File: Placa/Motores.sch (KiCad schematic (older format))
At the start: 11 parts, among them U1 DVR8833, U2 DVR8833

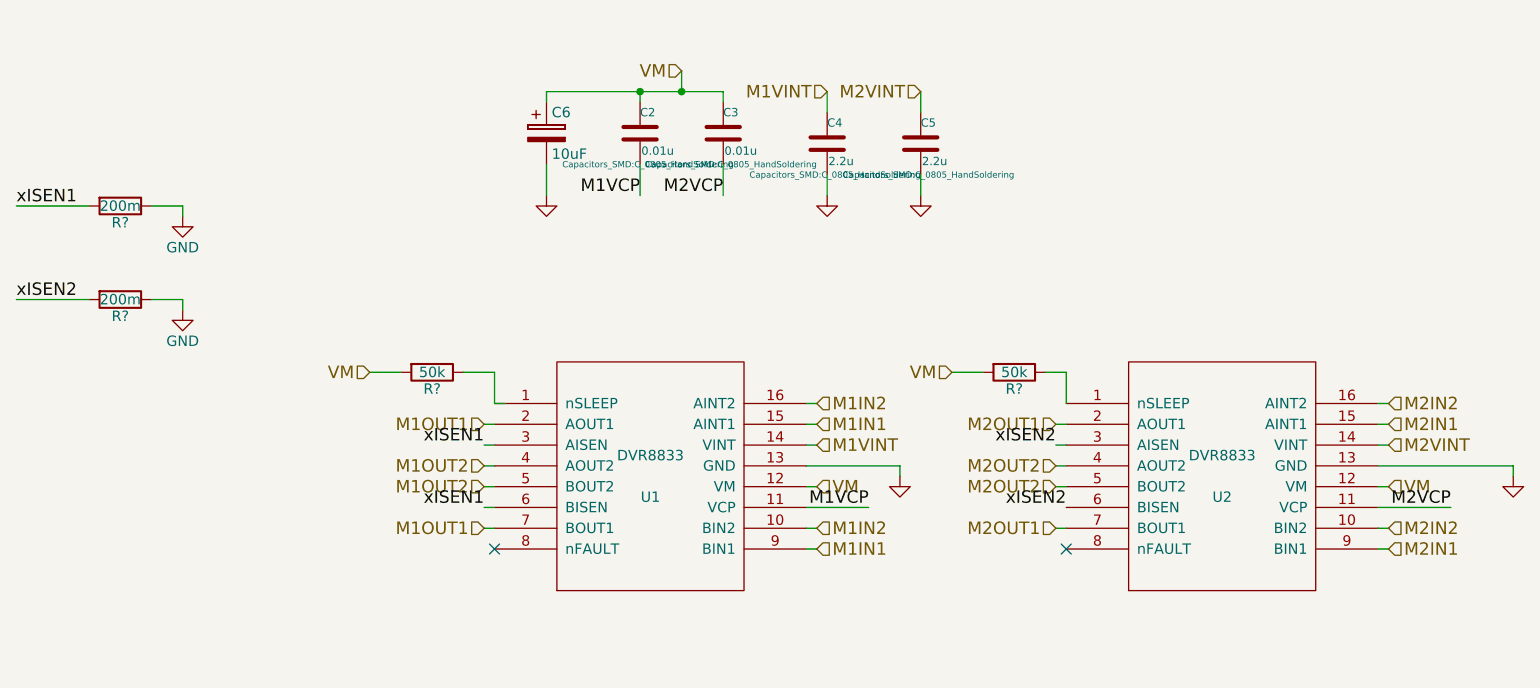
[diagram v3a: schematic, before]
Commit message: estan casi todas las cosas en su lugar, falta cambiar DVRs y regulador y rutear
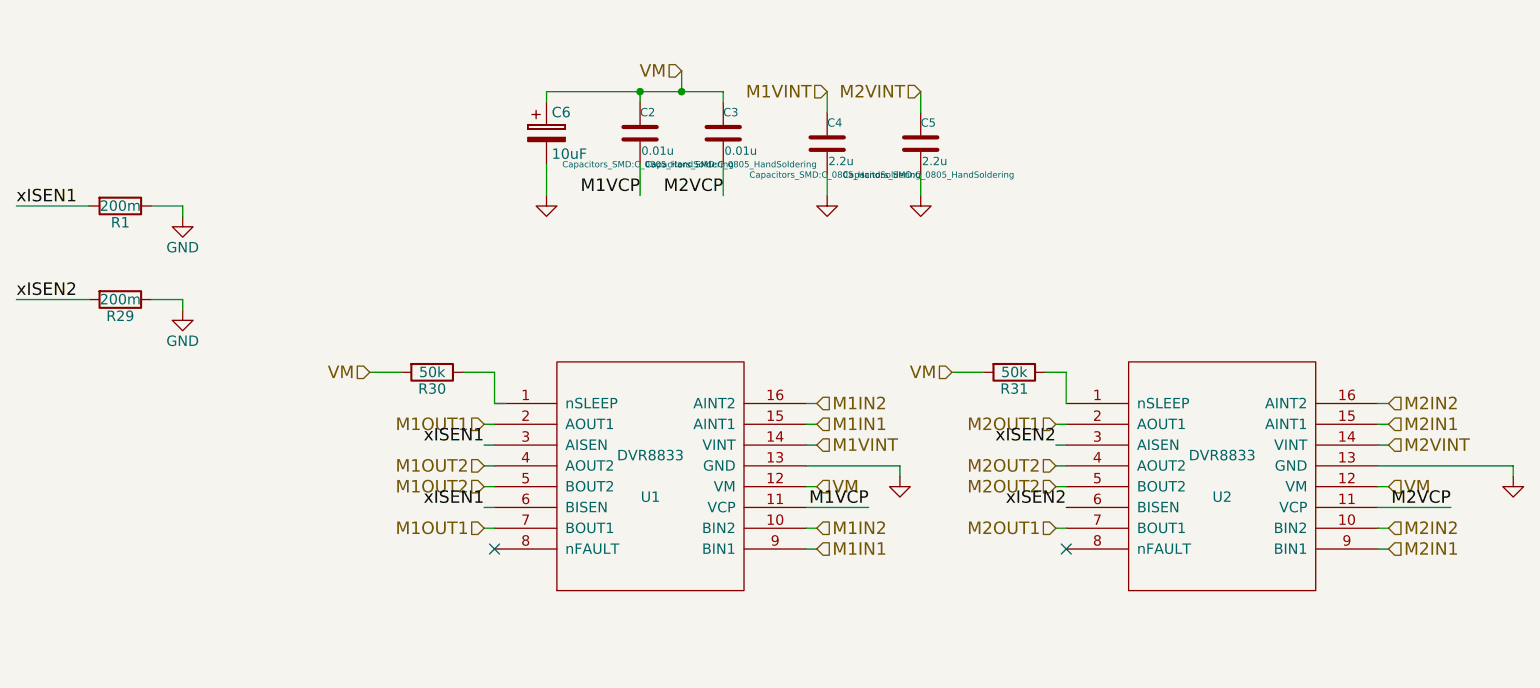
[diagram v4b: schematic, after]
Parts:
- gave numbers to parts that had none: 4
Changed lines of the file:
@@
 $EndComp
 $Comp
-L GND #PWR043
+L GND #PWR43
 U 1 1 55EB047B
 P 5600 3800
-F 0 "#PWR043" H 5600 3800 30  0001 C CNN
+F 0 "#PWR43" H 5600 3800 30  0001 C CNN
 F 1 "GND" H 5600 3730 30  0001 C CNN
 F 2 "" H 5600 3800 60  0000 C CNN
@@
 $EndComp
 $Comp
-L GND #PWR044
+L GND #PWR45
 U 1 1 55EB0487
 P 8550 3800
-F 0 "#PWR044" H 8550 3800 30  0001 C CNN
+F 0 "#PWR45" H 8550 3800 30  0001 C CNN
 F 1 "GND" H 8550 3730 30  0001 C CNN
 F 2 "" H 8550 3800 60  0000 C CNN
@@
 	4350 2300 4350 2450
 $Comp
-L GND #PWR045
+L GND #PWR41
 U 1 1 55EB1201
 P 3900 2450
-F 0 "#PWR045" H 3900 2450 30  0001 C CNN
+F 0 "#PWR41" H 3900 2450 30  0001 C CNN
 F 1 "GND" H 3900 2380 30  0001 C CNN
 F 2 "" H 3900 2450 60  0000 C CNN
@@
 $EndComp
 $Comp
-L GND #PWR046
+L GND #PWR42
 U 1 1 55EB12DF
 P 5250 2450
-F 0 "#PWR046" H 5250 2450 30  0001 C CNN
+F 0 "#PWR42" H 5250 2450 30  0001 C CNN
 F 1 "GND" H 5250 2380 30  0001 C CNN
 F 2 "" H 5250 2450 60  0000 C CNN
@@
 $EndComp
 $Comp
-L GND #PWR047
+L GND #PWR44
 U 1 1 55EB12E5
 P 5700 2450
-F 0 "#PWR047" H 5700 2450 30  0001 C CNN
+F 0 "#PWR44" H 5700 2450 30  0001 C CNN
 F 1 "GND" H 5700 2380 30  0001 C CNN
 F 2 "" H 5700 2450 60  0000 C CNN
@@
 xISEN1
 $Comp
-L R R?
+L R R1
 U 1 1 5748FFC9
 P 1850 2500
-F 0 "R?" V 1930 2500 50  0000 C CNN
+F 0 "R1" V 1930 2500 50  0000 C CNN
 F 1 "200m" V 1850 2500 50  0000 C CNN
 F 2 "" V 1780 2500 50  0000 C CNN
@@
 	2150 2500 2150 2550
 $Comp
-L GND #PWR?
+L GND #PWR39
 U 1 1 5749021E
 P 2150 2550
-F 0 "#PWR?" H 2150 2300 50  0001 C CNN
+F 0 "#PWR39" H 2150 2300 50  0001 C CNN
 F 1 "GND" H 2150 2400 50  0000 C CNN
 F 2 "" H 2150 2550 50  0000 C CNN
@@
 xISEN2
 $Comp
-L R R?
+L R R29
 U 1 1 574909EB
 P 1850 2950
-F 0 "R?" V 1930 2950 50  0000 C CNN
+F 0 "R29" V 1930 2950 50  0000 C CNN
 F 1 "200m" V 1850 2950 50  0000 C CNN
 F 2 "" V 1780 2950 50  0000 C CNN
@@
 	2150 2950 2150 3000
 $Comp
-L GND #PWR?
+L GND #PWR40
 U 1 1 574909F4
 P 2150 3000
-F 0 "#PWR?" H 2150 2750 50  0001 C CNN
+F 0 "#PWR40" H 2150 2750 50  0001 C CNN
 F 1 "GND" H 2150 2850 50  0000 C CNN
 F 2 "" H 2150 3000 50  0000 C CNN
@@
 	3650 3300 3500 3300
 $Comp
-L R R?
+L R R30
 U 1 1 57492D3E
 P 3350 3300
-F 0 "R?" V 3430 3300 50  0000 C CNN
+F 0 "R30" V 3430 3300 50  0000 C CNN
 F 1 "50k" V 3350 3300 50  0000 C CNN
 F 2 "" V 3280 3300 50  0000 C CNN
@@
 $EndComp
 $Comp
-L R R?
+L R R31
 U 1 1 5749308D
 P 6150 3300
-F 0 "R?" V 6230 3300 50  0000 C CNN
+F 0 "R31" V 6230 3300 50  0000 C CNN
 F 1 "50k" V 6150 3300 50  0000 C CNN
 F 2 "" V 6080 3300 50  0000 C CNN

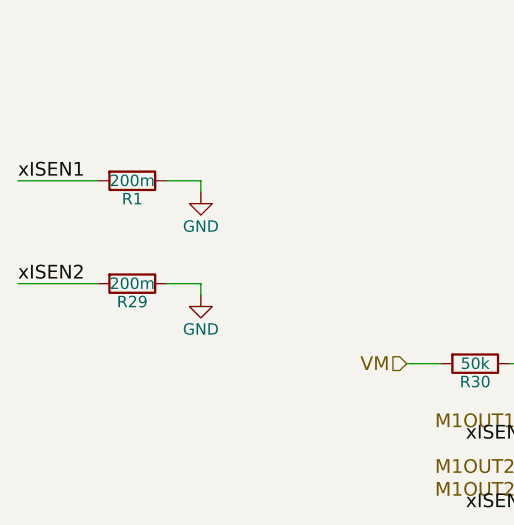
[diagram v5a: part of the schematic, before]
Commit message: Modificaciones a la placa
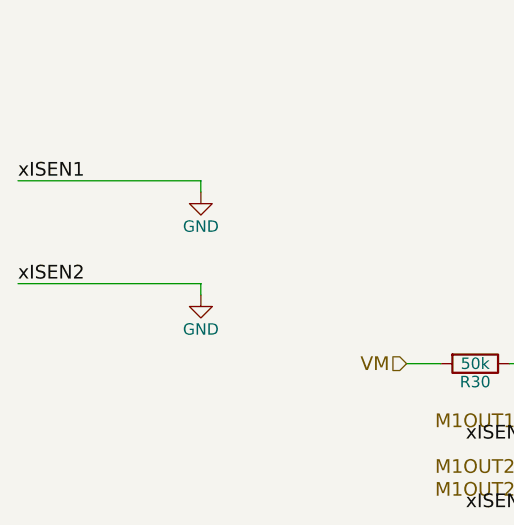
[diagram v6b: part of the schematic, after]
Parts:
- removed R1, R29: 200m, symbol R
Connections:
- net xISEN1 is gone; now on net GND: U1.3 (AISEN), U1.6 (BISEN)
- net xISEN2 is gone; now on net GND: U2.3 (AISEN), U2.6 (BISEN)
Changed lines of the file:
@@
 LIBS:reg_204-5
 LIBS:DVR8833
+LIBS:sn74lvc2g86
+LIBS:placa-cache
 EELAYER 25 0
 EELAYER END
 $Descr A4 11693 8268
 encoding utf-8
-Sheet 3 4
+Sheet 2 4
 Title ""
 Date "5 sep 2015"
@@
 $EndComp
 $Comp
-L GND #PWR43
+L GND #PWR040
 U 1 1 55EB047B
 P 5600 3800
-F 0 "#PWR43" H 5600 3800 30  0001 C CNN
+F 0 "#PWR040" H 5600 3800 30  0001 C CNN
 F 1 "GND" H 5600 3730 30  0001 C CNN
 F 2 "" H 5600 3800 60  0000 C CNN
@@
 $EndComp
 $Comp
-L GND #PWR45
+L GND #PWR041
 U 1 1 55EB0487
 P 8550 3800
-F 0 "#PWR45" H 8550 3800 30  0001 C CNN
+F 0 "#PWR041" H 8550 3800 30  0001 C CNN
 F 1 "GND" H 8550 3730 30  0001 C CNN
 F 2 "" H 8550 3800 60  0000 C CNN
@@
 	4350 2300 4350 2450
 $Comp
-L GND #PWR41
+L GND #PWR042
 U 1 1 55EB1201
 P 3900 2450
-F 0 "#PWR41" H 3900 2450 30  0001 C CNN
+F 0 "#PWR042" H 3900 2450 30  0001 C CNN
 F 1 "GND" H 3900 2380 30  0001 C CNN
 F 2 "" H 3900 2450 60  0000 C CNN
@@
 $EndComp
 $Comp
-L GND #PWR42
+L GND #PWR043
 U 1 1 55EB12DF
 P 5250 2450
-F 0 "#PWR42" H 5250 2450 30  0001 C CNN
+F 0 "#PWR043" H 5250 2450 30  0001 C CNN
 F 1 "GND" H 5250 2380 30  0001 C CNN
 F 2 "" H 5250 2450 60  0000 C CNN
@@
 $EndComp
 $Comp
-L GND #PWR44
+L GND #PWR044
 U 1 1 55EB12E5
 P 5700 2450
-F 0 "#PWR44" H 5700 2450 30  0001 C CNN
+F 0 "#PWR044" H 5700 2450 30  0001 C CNN
 F 1 "GND" H 5700 2380 30  0001 C CNN
 F 2 "" H 5700 2450 60  0000 C CNN
@@
 Text Label 3600 3950 2    60   ~ 0
 xISEN1
-$Comp
-L R R1
-U 1 1 5748FFC9
-P 1850 2500
-F 0 "R1" V 1930 2500 50  0000 C CNN
-F 1 "200m" V 1850 2500 50  0000 C CNN
-F 2 "" V 1780 2500 50  0000 C CNN
-F 3 "" H 1850 2500 50  0000 C CNN
-	1    1850 2500
-	0    1    1    0
-$EndComp
-Wire Wire Line
-	1350 2500 1700 2500
-Wire Wire Line
-	2000 2500 2150 2500
+Wire Wire Line
+	1350 2500 2150 2500
 Wire Wire Line
 	2150 2500 2150 2550
 $Comp
-L GND #PWR39
+L GND #PWR045
 U 1 1 5749021E
 P 2150 2550
-F 0 "#PWR39" H 2150 2300 50  0001 C CNN
+F 0 "#PWR045" H 2150 2300 50  0001 C CNN
 F 1 "GND" H 2150 2400 50  0000 C CNN
 F 2 "" H 2150 2550 50  0000 C CNN
@@
 Text Label 1350 2950 0    60   ~ 0
 xISEN2
-$Comp
-L R R29
-U 1 1 574909EB
-P 1850 2950
-F 0 "R29" V 1930 2950 50  0000 C CNN
-F 1 "200m" V 1850 2950 50  0000 C CNN
-F 2 "" V 1780 2950 50  0000 C CNN
-F 3 "" H 1850 2950 50  0000 C CNN
-	1    1850 2950
-	0    1    1    0
-$EndComp
-Wire Wire Line
-	1350 2950 1700 2950
-Wire Wire Line
-	2000 2950 2150 2950
+Wire Wire Line
+	1350 2950 2150 2950
 Wire Wire Line
 	2150 2950 2150 3000
 $Comp
-L GND #PWR40
+L GND #PWR046
 U 1 1 574909F4
 P 2150 3000
-F 0 "#PWR40" H 2150 2750 50  0001 C CNN
+F 0 "#PWR046" H 2150 2750 50  0001 C CNN
 F 1 "GND" H 2150 2850 50  0000 C CNN
 F 2 "" H 2150 3000 50  0000 C CNN

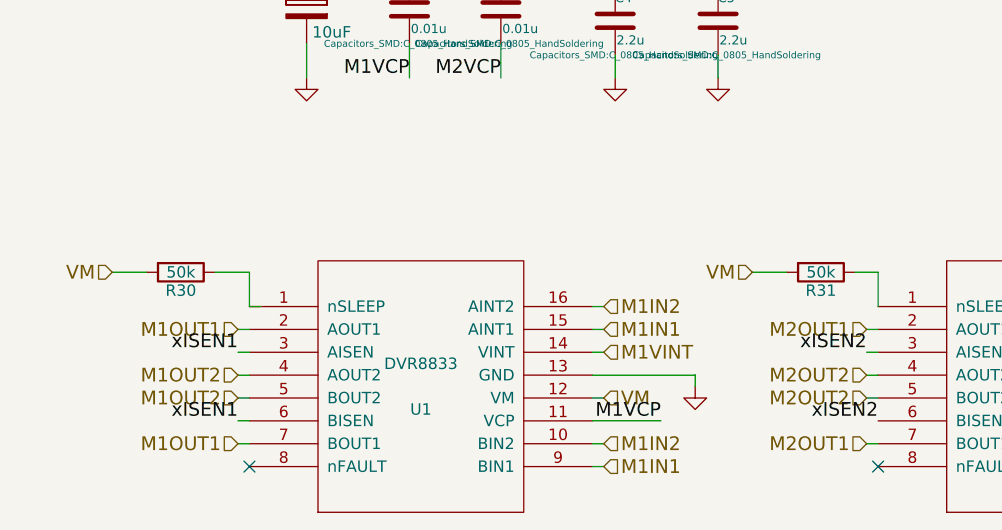
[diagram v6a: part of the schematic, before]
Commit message: se termino el esquematico y asociacion de componentes, falta acomodar y rutear PCB
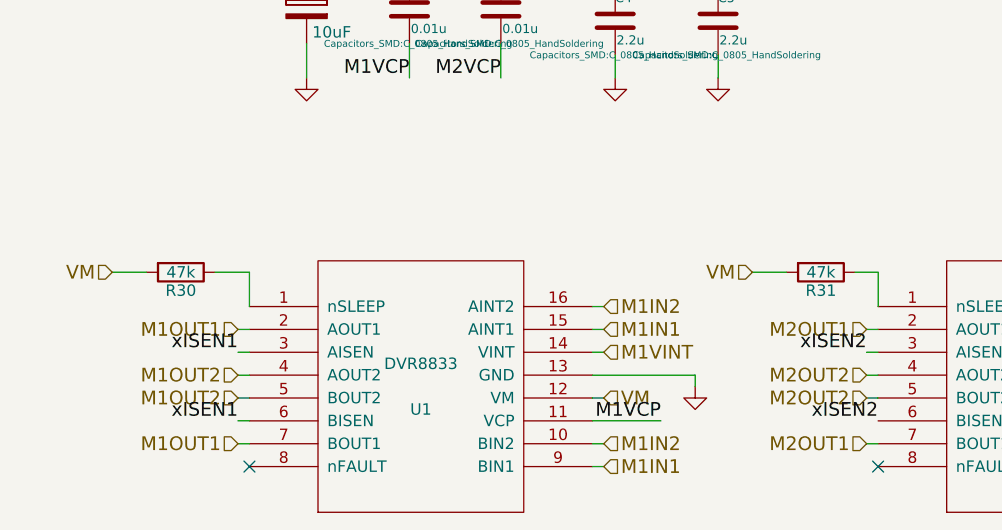
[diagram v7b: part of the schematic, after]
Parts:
- R30, R31: value 50k -> 47k; footprint (none) -> Resistors_SMD:R_0805_HandSoldering
- U1, U2: footprint Housings_SSOP:TSSOP-16_4.4x5mm_Pitch0.65mm -> Bibliotecas:TSSOP-16_4.4x5mm_Pitch0.65mm
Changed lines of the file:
@@
 F 0 "U1" H 4400 3700 50  0000 C CNN
 F 1 "DVR8833" H 4400 3900 50  0000 C CNN
-F 2 "Housings_SSOP:TSSOP-16_4.4x5mm_Pitch0.65mm" H 4400 3800 50  0001 C CNN
+F 2 "Bibliotecas:TSSOP-16_4.4x5mm_Pitch0.65mm" H 4400 3800 50  0001 C CNN
 F 3 "DOCUMENTATION" H 4400 3800 50  0001 C CNN
 	1    4400 3800
@@
 F 0 "U2" H 7150 3700 50  0000 C CNN
 F 1 "DVR8833" H 7150 3900 50  0000 C CNN
-F 2 "Housings_SSOP:TSSOP-16_4.4x5mm_Pitch0.65mm" H 7150 3800 50  0001 C CNN
+F 2 "Bibliotecas:TSSOP-16_4.4x5mm_Pitch0.65mm" H 7150 3800 50  0001 C CNN
 F 3 "DOCUMENTATION" H 7150 3800 50  0001 C CNN
 	1    7150 3800
@@
 NoConn ~ 6400 4150
 Wire Wire Line
-	3700 3450 3650 3450
-Wire Wire Line
 	3650 3450 3650 3300
 Wire Wire Line
@@
 P 3350 3300
 F 0 "R30" V 3430 3300 50  0000 C CNN
-F 1 "50k" V 3350 3300 50  0000 C CNN
-F 2 "" V 3280 3300 50  0000 C CNN
+F 1 "47k" V 3350 3300 50  0000 C CNN
+F 2 "Resistors_SMD:R_0805_HandSoldering" V 3280 3300 50  0001 C CNN
 F 3 "" H 3350 3300 50  0000 C CNN
 	1    3350 3300
@@
 P 6150 3300
 F 0 "R31" V 6230 3300 50  0000 C CNN
-F 1 "50k" V 6150 3300 50  0000 C CNN
-F 2 "" V 6080 3300 50  0000 C CNN
+F 1 "47k" V 6150 3300 50  0000 C CNN
+F 2 "Resistors_SMD:R_0805_HandSoldering" V 6080 3300 50  0001 C CNN
 F 3 "" H 6150 3300 50  0000 C CNN
 	1    6150 3300

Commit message: Está todo ruteado, falta engrozar pistas, chequear wiki y un chequeo general
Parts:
- C6: footprint Capacitors_ThroughHole:C_Radial_D5_L11_P2.5 -> Capacitors_SMD:C_0805_HandSoldering
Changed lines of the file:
@@
 F 0 "C6" H 3925 2250 50  0000 L CNN
 F 1 "10uF" H 3925 2050 50  0000 L CNN
-F 2 "Capacitors_ThroughHole:C_Radial_D5_L11_P2.5" H 3938 2000 50  0001 C CNN
+F 2 "Capacitors_SMD:C_0805_HandSoldering" H 3938 2000 50  0001 C CNN
 F 3 "" H 3900 2150 50  0000 C CNN
 	1    3900 2150
